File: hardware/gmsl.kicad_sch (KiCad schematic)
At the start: 17 parts, among them U1 MAX96717GTJ/VY+

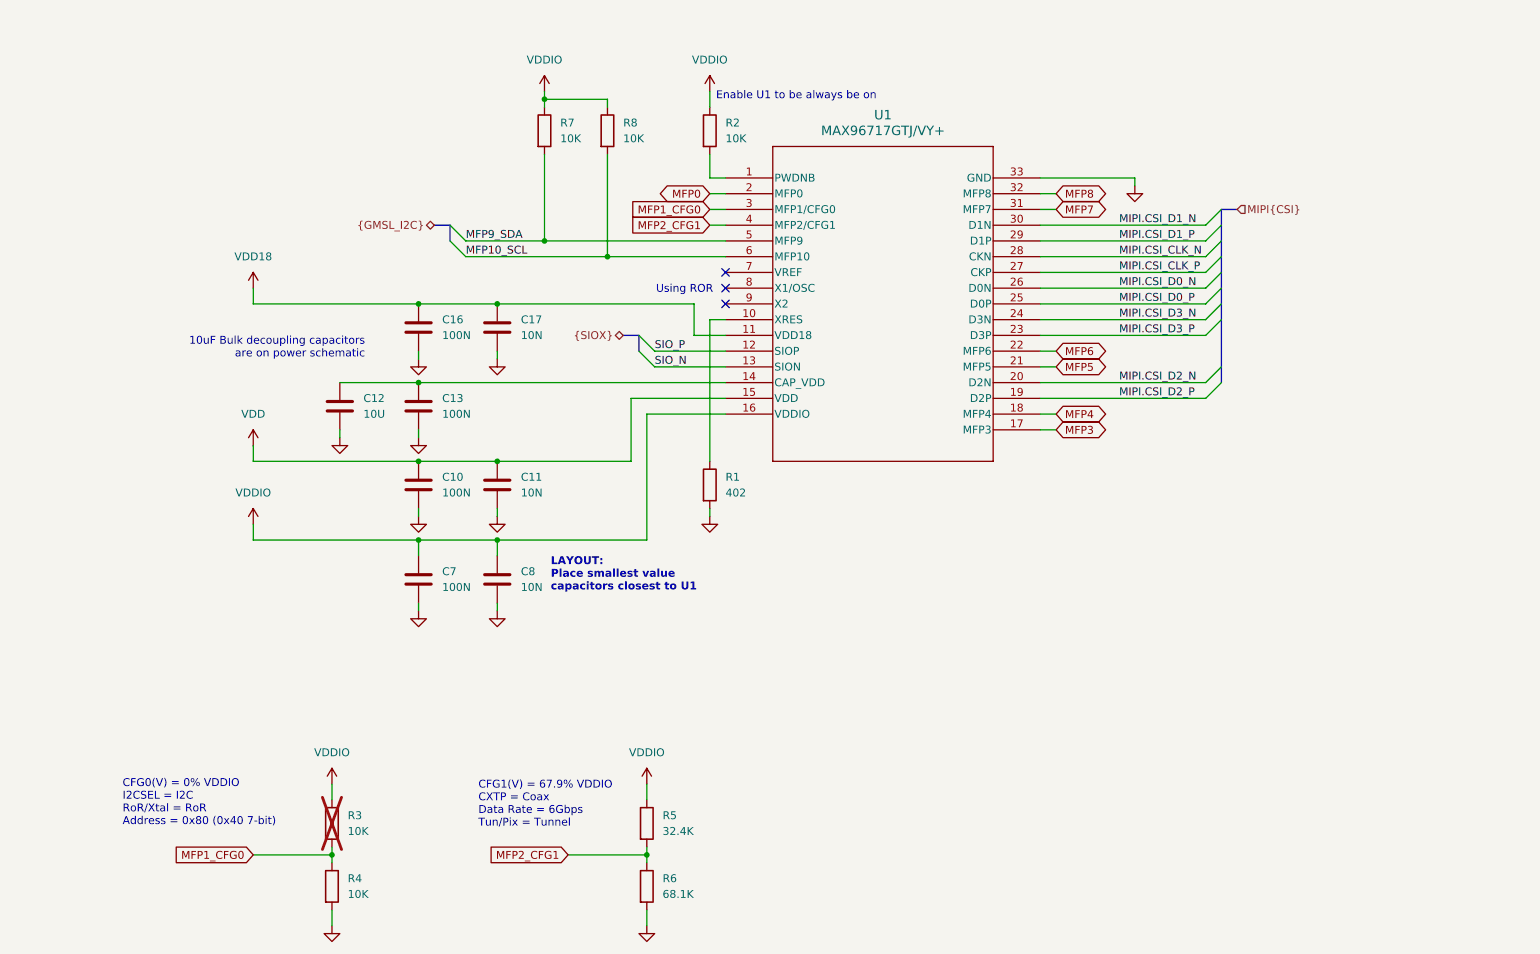
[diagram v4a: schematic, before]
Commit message: finished schematic, changed to 4 layer board
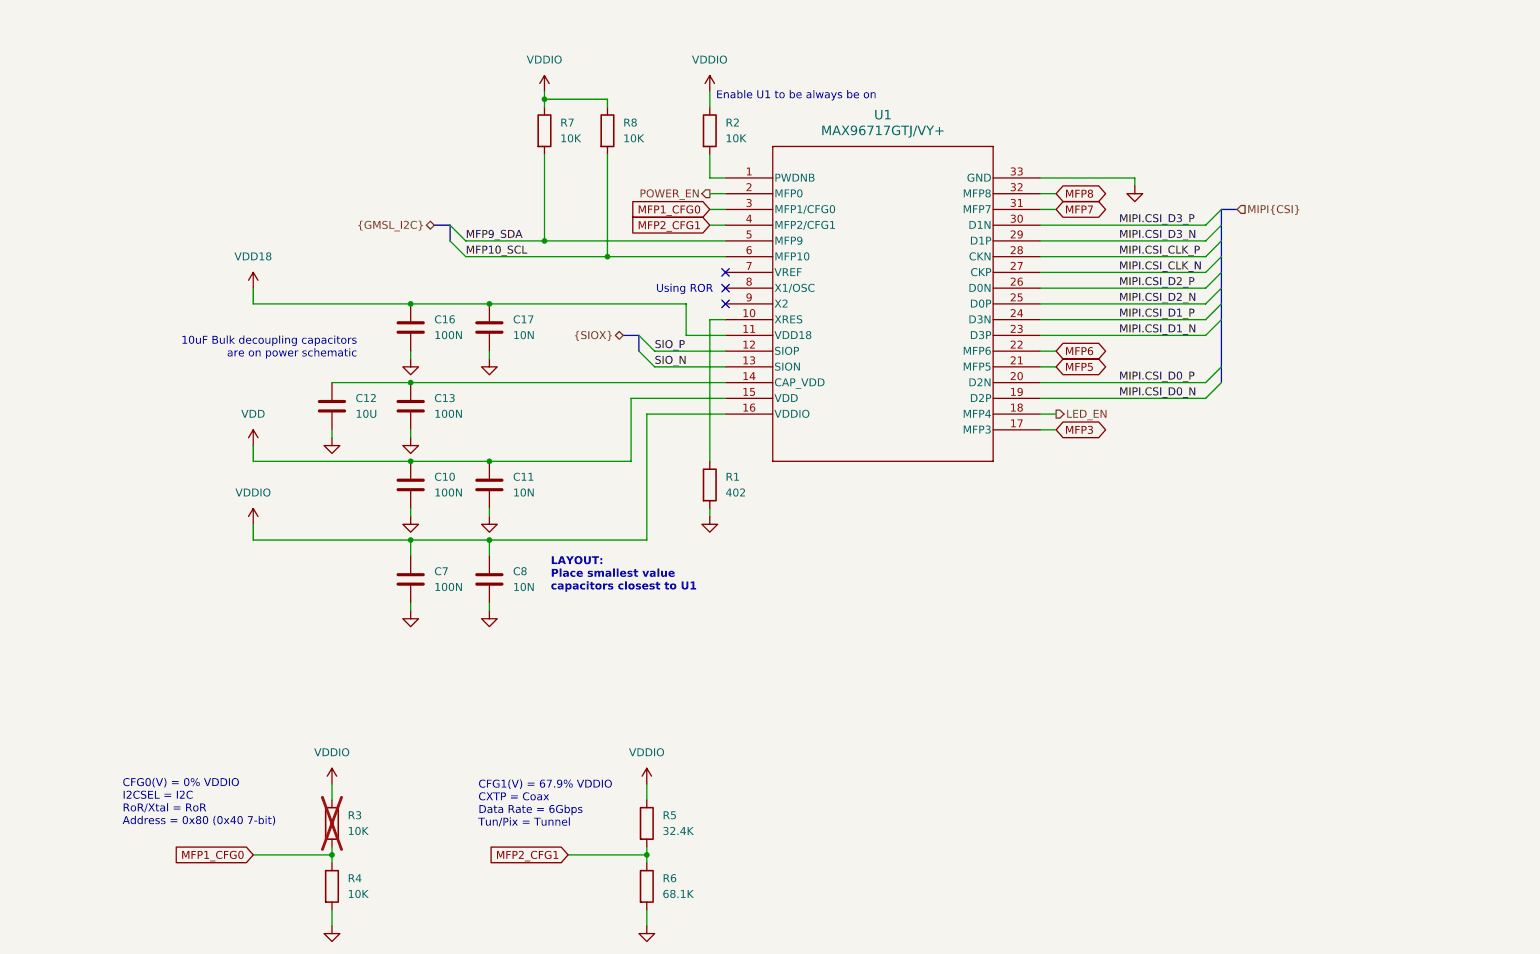
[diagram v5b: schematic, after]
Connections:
- net MIPI.CSI_CLK_N: now also U1.27 (CKP); no longer U1.28 (CKN)
- net MIPI.CSI_CLK_P: now also U1.28 (CKN); no longer U1.27 (CKP)
- net MIPI.CSI_D0_N: now also U1.19 (D2P); no longer U1.26 (D0N)
- net MIPI.CSI_D0_P: now also U1.20 (D2N); no longer U1.25 (D0P)
- net MIPI.CSI_D1_N: now also U1.23 (D3P); no longer U1.30 (D1N)
- net MIPI.CSI_D1_P: now also U1.24 (D3N); no longer U1.29 (D1P)
- net MIPI.CSI_D2_N: now also U1.25 (D0P); no longer U1.20 (D2N)
- net MIPI.CSI_D2_P: now also U1.26 (D0N); no longer U1.19 (D2P)
- net MIPI.CSI_D3_N: now also U1.29 (D1P); no longer U1.24 (D3N)
- net MIPI.CSI_D3_P: now also U1.30 (D1N); no longer U1.23 (D3P)
- net MFP0 renamed POWER_EN
- net MFP4 renamed LED_EN
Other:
- moved on the sheet: C10, C11, C12, C13, C16, C17, C7, C8

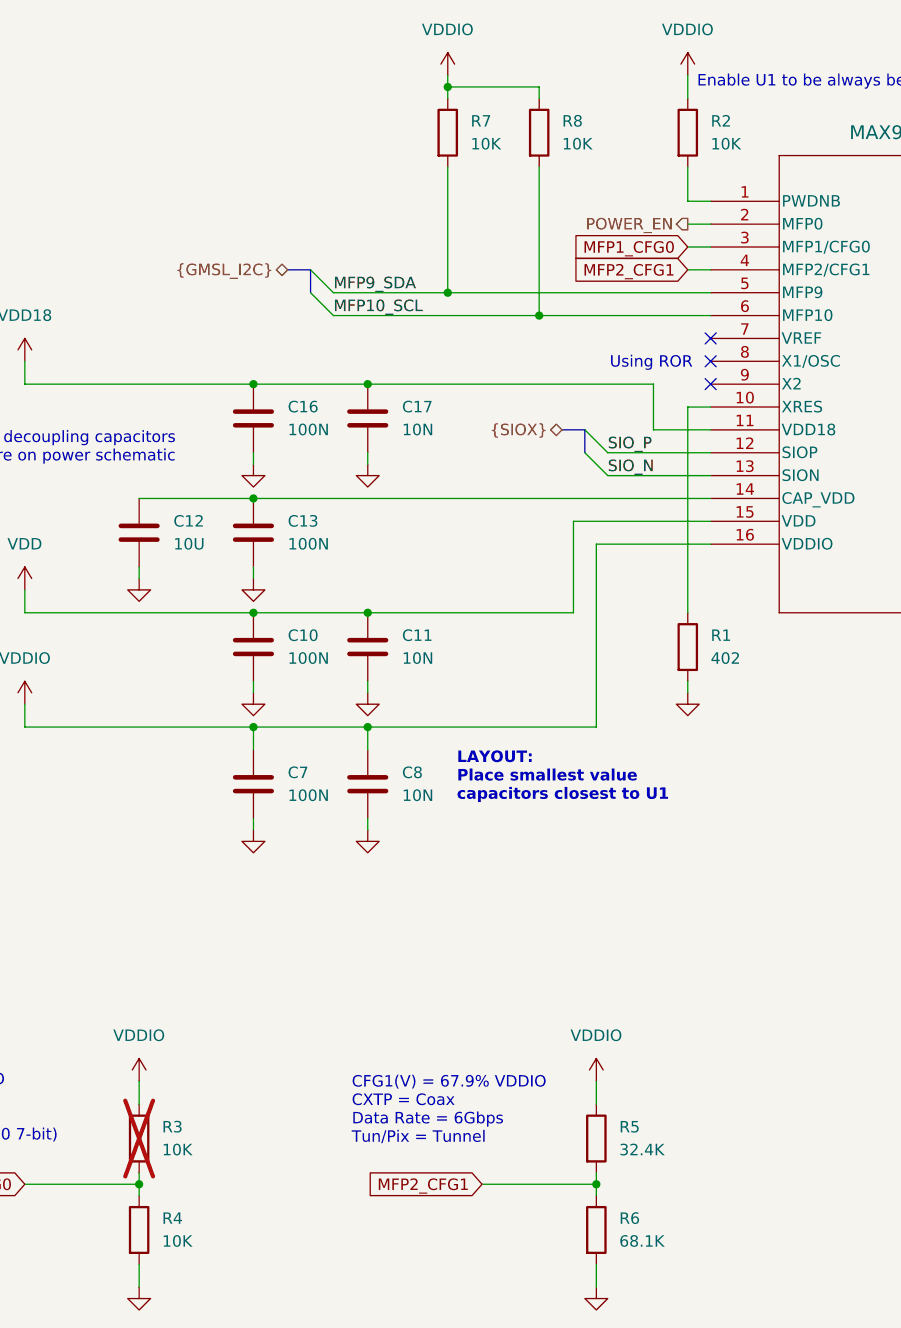
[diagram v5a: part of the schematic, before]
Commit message: layout planning and decided to use bottom layer for components
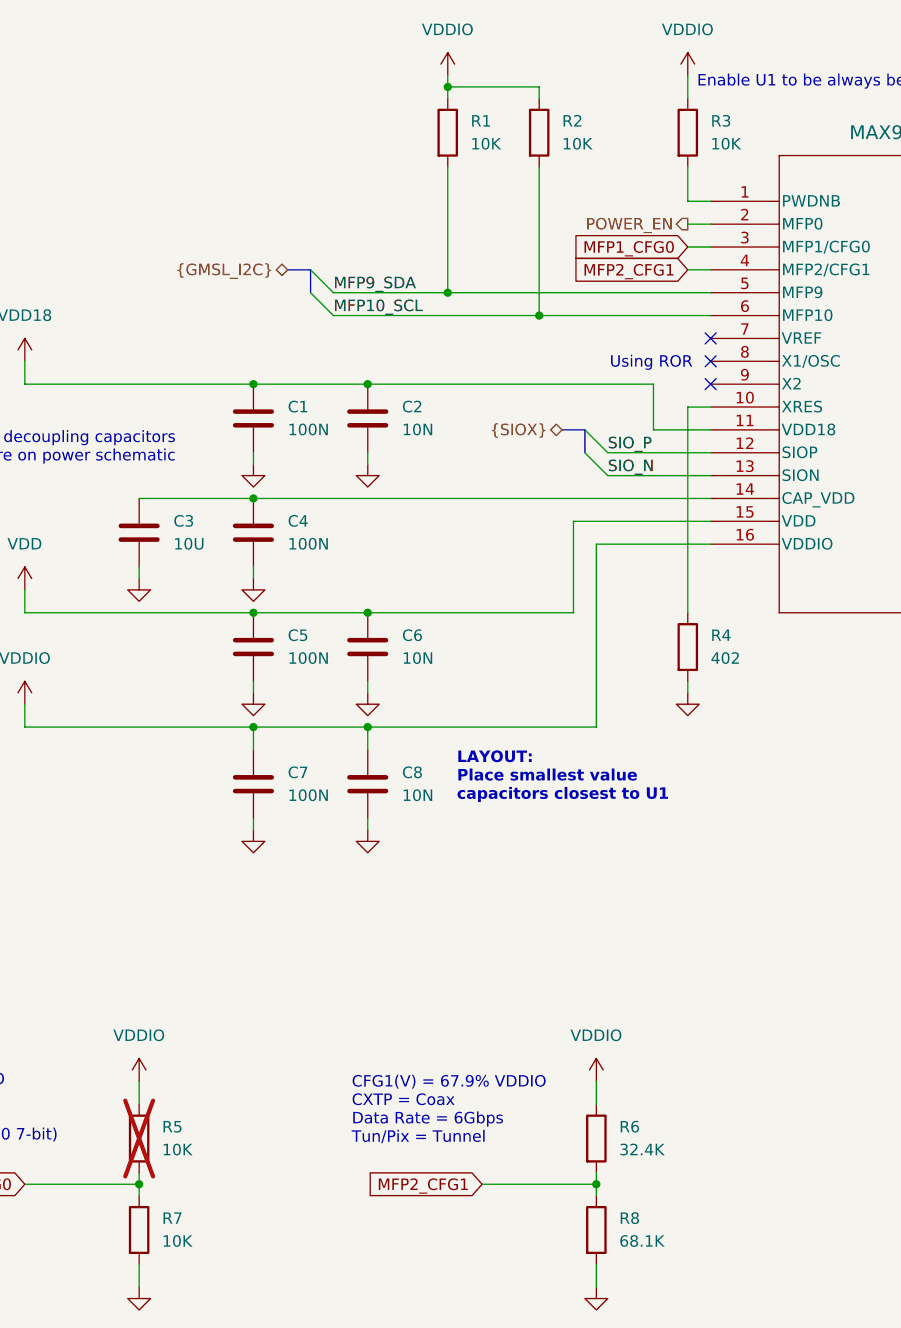
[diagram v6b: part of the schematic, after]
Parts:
- renumbered C16 to C1, C17 to C2, C12 to C3, C13 to C4, C10 to C5, C11 to C6, R7 to R1, R8 to R2, R2 to R3, R1 to R4, R3 to R5, R5 to R6, R4 to R7, R6 to R8

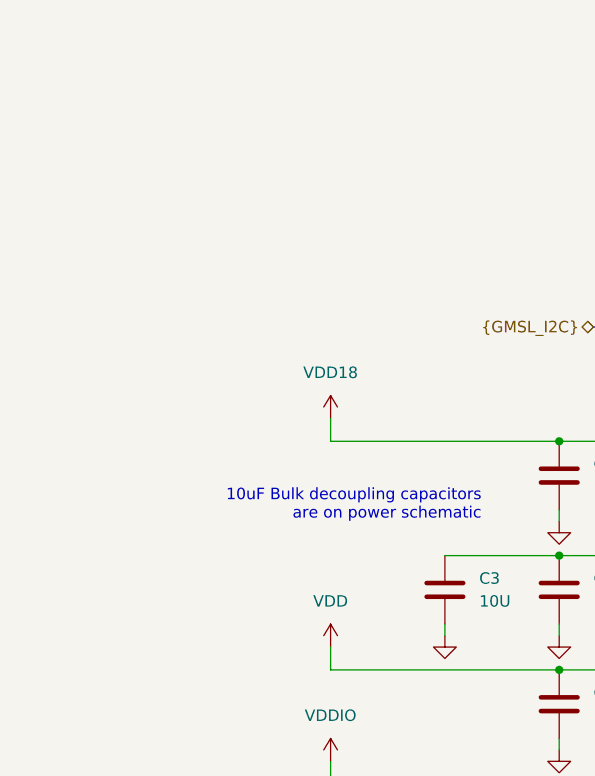
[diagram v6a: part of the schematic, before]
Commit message: cleaned up power supply and started minor power plane routing
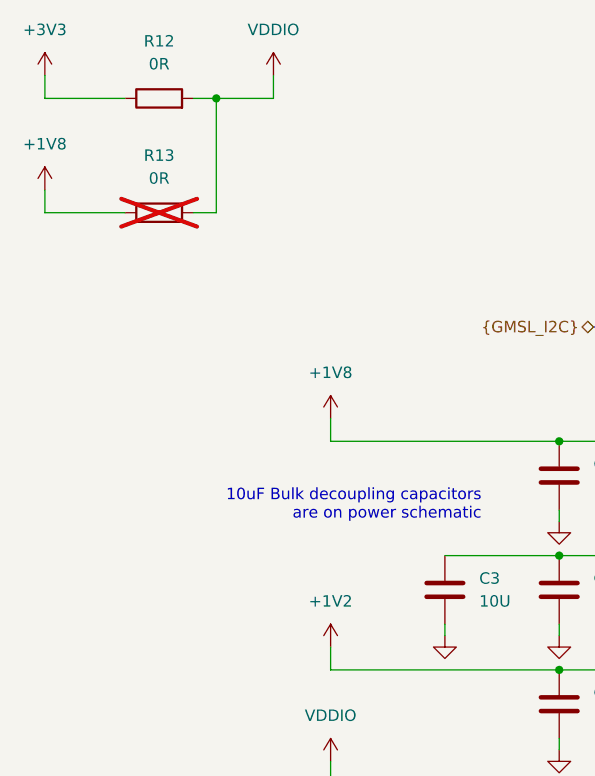
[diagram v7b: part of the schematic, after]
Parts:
- added R12, R13: 0R, Resistor_SMD:R_0402_1005Metric, symbol Device:R
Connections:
- net VDDIO: now also R12.2, R13.2
- net VDD renamed +1V2
- net VDD18 renamed +1V8
- net +1V8: now also R13.1
- new net +3V3: R12.1

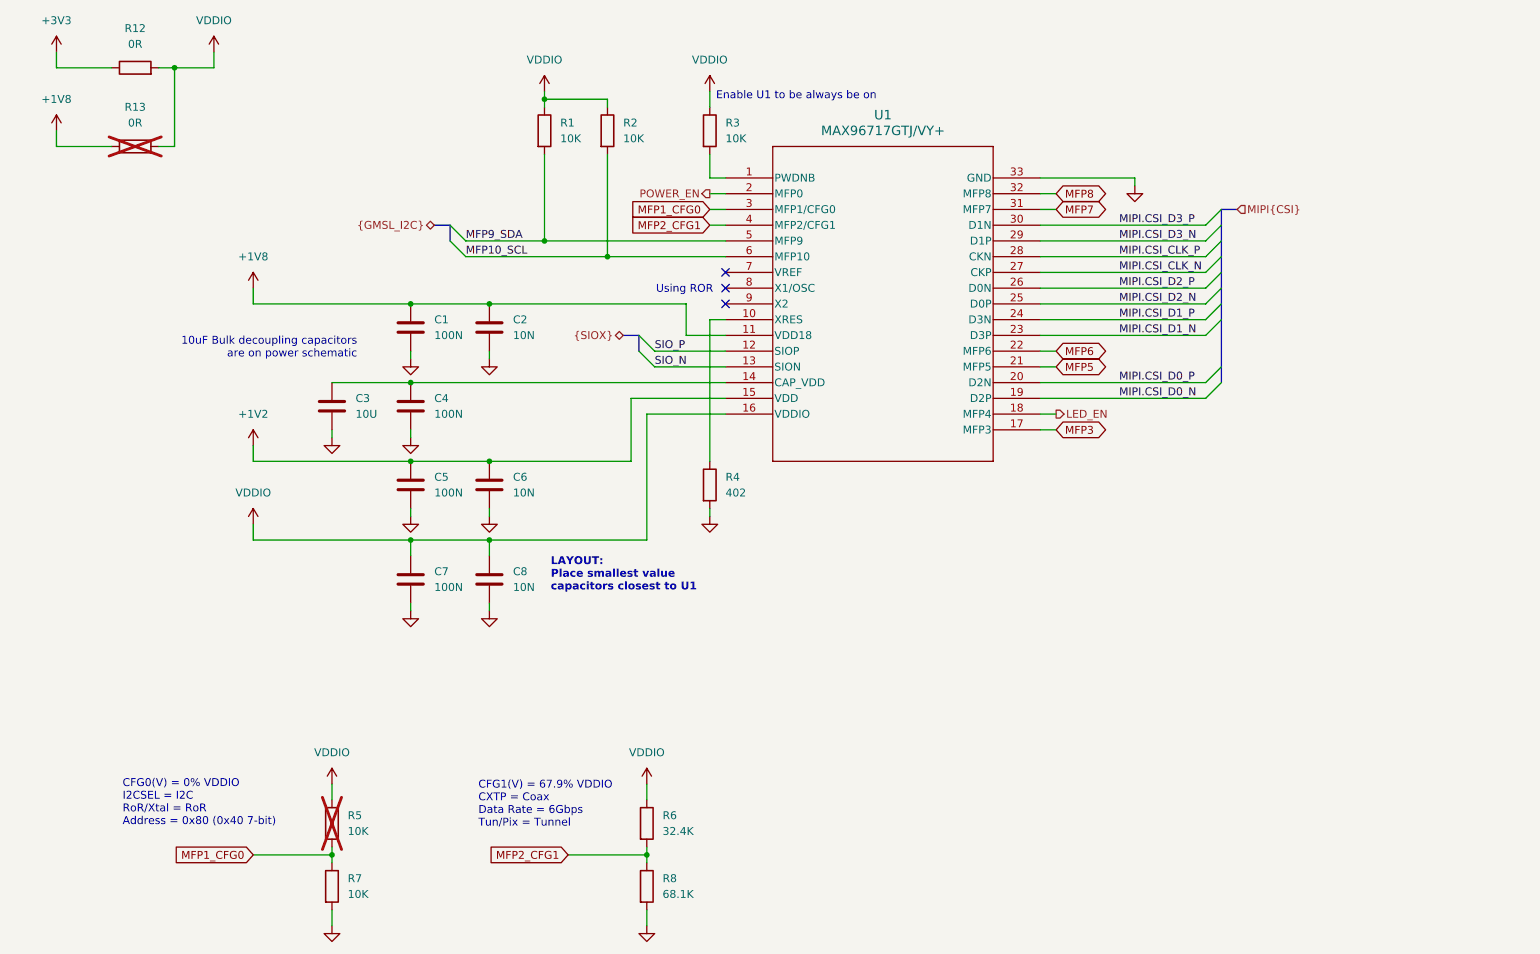
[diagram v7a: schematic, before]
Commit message: added LED circuits and test points on extra MFPs
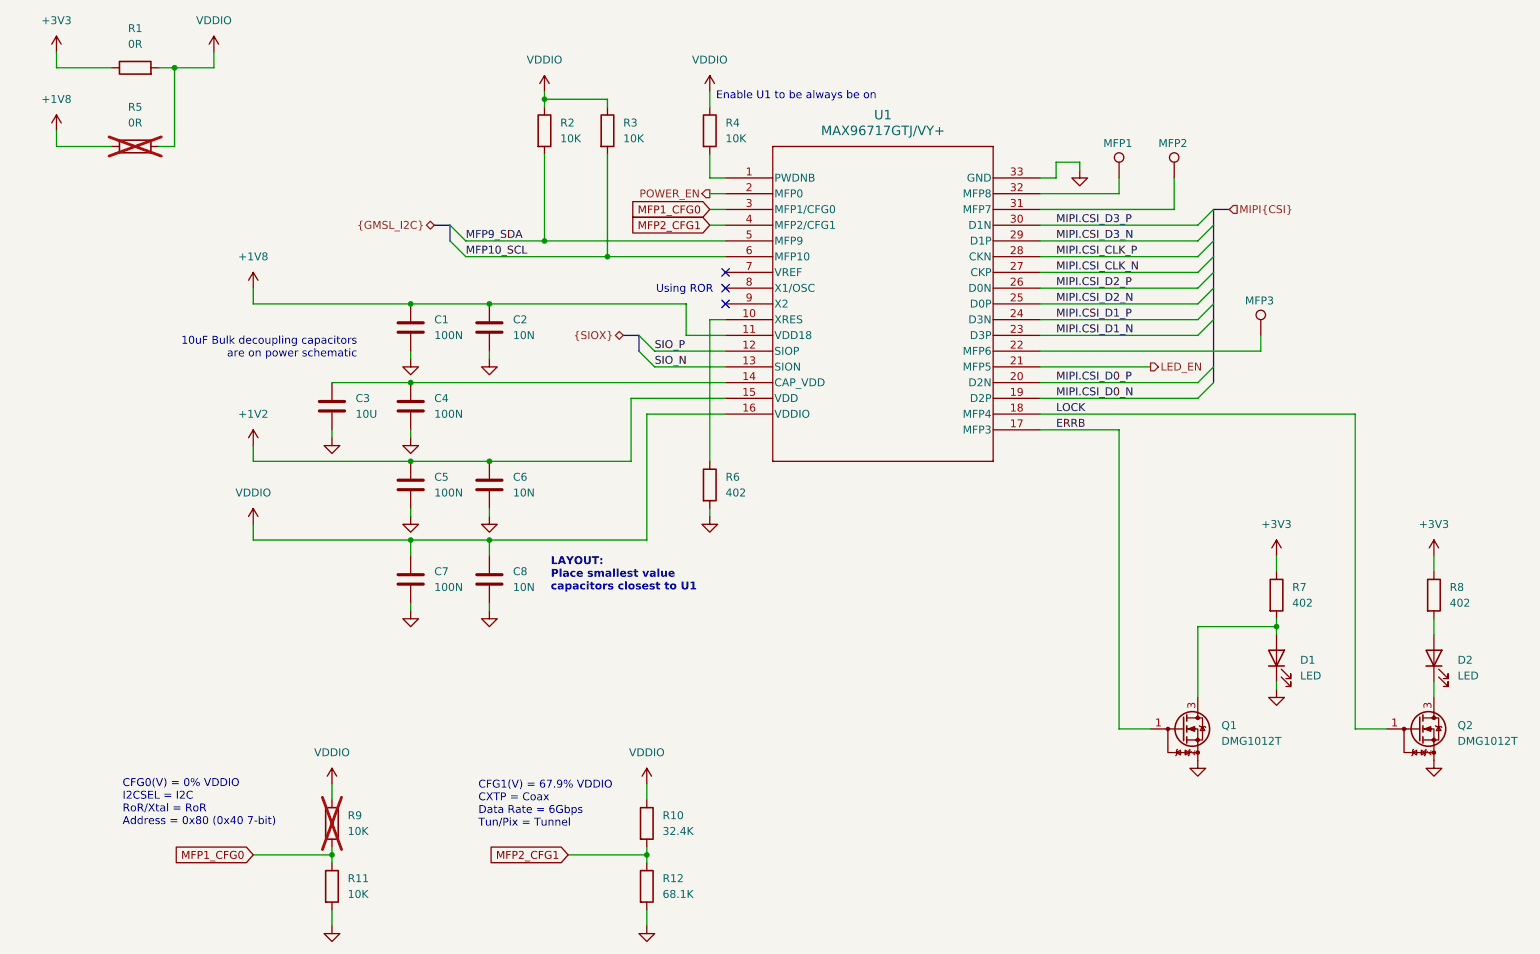
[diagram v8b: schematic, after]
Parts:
- added D1, D2: LED, LED_SMD:LED_0603_1608Metric, symbol Device:LED
- added MFP1, MFP2, MFP3: TestPoint, Connector_Pin:Pin_D1.0mm_L10.0mm, symbol Connector:TestPoint
- added Q1, Q2: DMG1012T, Package_TO_SOT_SMD:SOT-523, symbol Transistor_FET:DMG1012T
- added R7, R8: 402, Resistor_SMD:R_0402_1005Metric, symbol Device:R
- renumbered R12 to R1, R6 to R10, R7 to R11, R8 to R12, R1 to R2, R2 to R3, R3 to R4, R13 to R5, R4 to R6, R5 to R9
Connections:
- net MFP5 is gone; now on net LED_EN: U1.21 (MFP5)
- net +3V3: now also R7.1, R8.1
- net GND: now also D1.1 (K), Q1.2 (S), Q2.2 (S)
- net LED_EN: no longer U1.18 (MFP4)
- net MFP3 renamed ERRB
- net ERRB: now also Q1.1 (G)
- net MFP6: no longer names the net of U1.22 (MFP6)
- net MFP6: now also MFP3.1
- net MFP7: no longer names the net of U1.31 (MFP7)
- net MFP7: now also MFP2.1
- net MFP8: no longer names the net of U1.32 (MFP8)
- net MFP8: now also MFP1.1
- new net: D1.2 (A), Q1.3 (D), R7.2
- new net: D2.1 (K), Q2.3 (D)
- new net: D2.2 (A), R8.2
- new net LOCK: Q2.1 (G), U1.18 (MFP4)
